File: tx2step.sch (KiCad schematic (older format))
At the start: 59 parts, among them CON1 BARREL_JACK, IC1 TPS2113A, IC3 MCP73831, IC4 TPS61202, IC5 DRV8834, IC6 DRV8834, J1 8P8C, J2 6P4C, J3 6P4C, J4 Debug, SW1 SW_DIP_x02, SW2 SW_DPDT_x2, SW3 SW_SPDT_MSM, U1 ATmega328P-MMH, Y1 16 MHz

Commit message: Use SPST for power switch
Add pullup resistor, unit is powered on when switch is open; off
when closed.
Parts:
- removed SW2: SW_DPDT_x2, symbol tx2step-rescue:SW_DPDT_x2
- added R4: 4.7KΩ, symbol Device:R_Small
- added SW2: SW_SPST, symbol Switch:SW_SPST
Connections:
- wire segments 287 -> 288
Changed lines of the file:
@@
-$EndComp
-$Comp
-L tx2step-rescue:SW_DPDT_x2 SW2
-U 1 1 58BE4643
-P 3700 6400
-F 0 "SW2" H 3700 6570 50  0000 C CNN
-F 1 "SW_DPDT_x2" H 3700 6200 50  0000 C CNN
-F 2 "" H 3700 6400 50  0001 C CNN
-F 3 "" H 3700 6400 50  0001 C CNN
-	1    3700 6400
-	-1   0    0    -1
 $EndComp
 $Comp
@@
 	3250 6550 3250 6500
 Wire Wire Line
-	3100 6800 3500 6800
-Wire Wire Line
 	3100 6550 3100 6800
 Connection ~ 4100 6800
@@
 Wire Wire Line
 	3900 6400 4300 6400
-Wire Wire Line
-	3500 6500 3500 6800
 Wire Wire Line
 	4700 5750 4200 5750
@@
 Connection ~ 6200 6300
 Wire Wire Line
-	3500 6800 4100 6800
-Connection ~ 3500 6800
-Wire Wire Line
-	3500 6300 3500 6200
-Connection ~ 3500 6200
-Wire Wire Line
 	2800 1800 2950 1800
 Wire Wire Line
@@
 	4200 6800 4300 6800
 Wire Wire Line
-	3250 6200 3500 6200
-Wire Wire Line
 	2950 6200 3250 6200
 Wire Wire Line
@@
 Wire Wire Line
 	6200 6300 6400 6300
-Wire Wire Line
-	3500 6200 4050 6200
 Wire Wire Line
 	2950 1800 3050 1800
@@
 Text Label 2700 4250 0    60   ~ 0
 DC_SENSE
+Wire Wire Line
+	3100 6800 3500 6800
+$Comp
+L Switch:SW_SPST SW2
+U 1 1 6347EBFA
+P 3700 6700
+F 0 "SW2" H 3700 6935 50  0000 C CNN
+F 1 "SW_SPST" H 3700 6844 50  0000 C CNN
+F 2 "" H 3700 6700 50  0001 C CNN
+F 3 "~" H 3700 6700 50  0001 C CNN
+	1    3700 6700
+	1    0    0    -1
+$EndComp
+Wire Wire Line
+	3900 6400 3900 6700
+Wire Wire Line
+	3500 6700 3500 6800
+Connection ~ 3500 6800
+Wire Wire Line
+	3500 6800 4100 6800
+Wire Wire Line
+	3250 6200 3500 6200
+$Comp
+L Device:R_Small R4
+U 1 1 635AA68E
+P 3500 6300
+F 0 "R4" H 3559 6346 50  0000 L CNN
+F 1 "4.7KΩ" H 3559 6255 50  0000 L CNN
+F 2 "" H 3500 6300 50  0001 C CNN
+F 3 "~" H 3500 6300 50  0001 C CNN
+	1    3500 6300
+	1    0    0    -1
+$EndComp
+Connection ~ 3500 6200
+Wire Wire Line
+	3500 6200 4050 6200
+Wire Wire Line
+	3500 6400 3900 6400
+Connection ~ 3900 6400
 $EndSCHEMATC

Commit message: Replace switches with pin header
This allows the switches to be mounted on the chassis, freeing up
space on the board and allowing for component flexibility.
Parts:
- removed RV1: POT, symbol tx2step-rescue:POT
- removed SW2: SW_SPST, symbol Switch:SW_SPST
- removed SW3: SW_SPDT_MSM, symbol tx2step-rescue:SW_SPDT_MSM
- added J5: CHASSIS_SWITCHES, symbol Connector_Generic:Conn_02x04_Odd_Even
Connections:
- net labels added: SW_POWER
- wire segments 288 -> 295
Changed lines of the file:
@@
-$EndComp
-$Comp
-L tx2step-rescue:SW_SPDT_MSM SW3
-U 1 1 58B86814
-P 5100 1000
-F 0 "SW3" H 5100 1200 50  0000 C CNN
-F 1 "SW_SPDT_MSM" H 5100 800 50  0000 C CNN
-F 2 "" H 5100 1000 50  0001 C CNN
-F 3 "" H 5100 1000 50  0001 C CNN
-	1    5100 1000
-	1    0    0    -1
-$EndComp
-$Comp
-L tx2step-rescue:POT RV1
-U 1 1 58B868AD
-P 5950 1000
-F 0 "RV1" V 5775 1000 50  0000 C CNN
-F 1 "POT" V 5850 1000 50  0000 C CNN
-F 2 "" H 5950 1000 50  0000 C CNN
-F 3 "" H 5950 1000 50  0000 C CNN
-	1    5950 1000
-	1    0    0    -1
-$EndComp
-$Comp
-L tx2step-rescue:GND #PWR025
-U 1 1 58B87520
-P 5950 1150
-F 0 "#PWR025" H 5950 900 50  0001 C CNN
-F 1 "GND" H 5950 1000 50  0000 C CNN
-F 2 "" H 5950 1150 50  0000 C CNN
-F 3 "" H 5950 1150 50  0000 C CNN
-	1    5950 1150
-	1    0    0    -1
 $EndComp
 $Comp
@@
 Connection ~ 2950 6200
 Wire Wire Line
-	3900 6400 4300 6400
-Wire Wire Line
 	4700 5750 4200 5750
 Wire Wire Line
@@
 Wire Wire Line
 	2000 850  2000 950
-$Comp
-L power:VCC #PWR024
-U 1 1 5FE50164
-P 5950 850
-F 0 "#PWR024" H 5950 700 50  0001 C CNN
-F 1 "VCC" H 5965 1023 50  0000 C CNN
-F 2 "" H 5950 850 50  0001 C CNN
-F 3 "" H 5950 850 50  0001 C CNN
-	1    5950 850
-	1    0    0    -1
-$EndComp
 $Comp
 L power:VCC #PWR032
@@
 	1    0    0    -1
 $EndComp
-Wire Wire Line
-	4700 1000 4900 1000
 Connection ~ 4700 1000
 $Comp
@@
 Wire Wire Line
 	4550 1000 4700 1000
-Wire Wire Line
-	6100 1000 6250 1000
-Text Label 6250 1000 0    60   ~ 0
-GUIDE_RATE
 Text Label 4550 1000 2    60   ~ 0
 TRACK_RATE
@@
 	1    0    0    -1
 $EndComp
-Wire Wire Line
-	5300 900  5400 900
-Wire Wire Line
-	5400 900  5400 850
-Wire Wire Line
-	5300 1100 5400 1100
-Wire Wire Line
-	5400 1100 5400 1250
-$Comp
-L power:GND #PWR031
-U 1 1 6325C28F
-P 5400 1250
-F 0 "#PWR031" H 5400 1000 50  0001 C CNN
-F 1 "GND" H 5405 1077 50  0000 C CNN
-F 2 "" H 5400 1250 50  0001 C CNN
-F 3 "" H 5400 1250 50  0001 C CNN
-	1    5400 1250
-	1    0    0    -1
-$EndComp
-$Comp
-L power:VCC #PWR022
-U 1 1 6325D155
-P 5400 850
-F 0 "#PWR022" H 5400 700 50  0001 C CNN
-F 1 "VCC" H 5415 1023 50  0000 C CNN
-F 2 "" H 5400 850 50  0001 C CNN
-F 3 "" H 5400 850 50  0001 C CNN
-	1    5400 850
-	1    0    0    -1
-$EndComp
 Connection ~ 2000 950
 Connection ~ 2000 1150
@@
 Text Label 2700 4250 0    60   ~ 0
 DC_SENSE
-Wire Wire Line
-	3100 6800 3500 6800
-$Comp
-L Switch:SW_SPST SW2
-U 1 1 6347EBFA
-P 3700 6700
-F 0 "SW2" H 3700 6935 50  0000 C CNN
-F 1 "SW_SPST" H 3700 6844 50  0000 C CNN
-F 2 "" H 3700 6700 50  0001 C CNN
-F 3 "~" H 3700 6700 50  0001 C CNN
-	1    3700 6700
-	1    0    0    -1
-$EndComp
-Wire Wire Line
-	3900 6400 3900 6700
-Wire Wire Line
-	3500 6700 3500 6800
-Connection ~ 3500 6800
-Wire Wire Line
-	3500 6800 4100 6800
 Wire Wire Line
 	3250 6200 3500 6200
@@
 Wire Wire Line
 	3500 6200 4050 6200
+$Comp
+L Connector_Generic:Conn_02x04_Odd_Even J5
+U 1 1 635FE306
+P 5950 1000
+F 0 "J5" H 6000 1317 50  0000 C CNN
+F 1 "CHASSIS_SWITCHES" H 6000 1226 50  0000 C CNN
+F 2 "" H 5950 1000 50  0001 C CNN
+F 3 "~" H 5950 1000 50  0001 C CNN
+	1    5950 1000
+	1    0    0    -1
+$EndComp
+Wire Wire Line
+	6250 1000 6350 1000
+Wire Wire Line
+	5750 1000 5650 1000
+Text Label 6350 1000 0    60   ~ 0
+GUIDE_RATE
+Text Label 5650 1000 2    60   ~ 0
+TRACK_RATE
+Text Label 6350 1200 0    60   ~ 0
+SW_POWER
+Wire Wire Line
+	6350 1200 6250 1200
+Wire Wire Line
+	5750 1200 5650 1200
+$Comp
+L power:GND #PWR025
+U 1 1 636F7BE1
+P 5650 1200
+F 0 "#PWR025" H 5650 950 50  0001 C CNN
+F 1 "GND" H 5655 1027 50  0000 C CNN
+F 2 "" H 5650 1200 50  0001 C CNN
+F 3 "" H 5650 1200 50  0001 C CNN
+	1    5650 1200
+	1    0    0    -1
+$EndComp
+Wire Wire Line
+	6250 900  6450 900
+Wire Wire Line
+	6450 900  6450 650
+Wire Wire Line
+	6450 650  6550 650
+Wire Wire Line
+	5750 900  5550 900
+Wire Wire Line
+	5550 900  5550 650
+Wire Wire Line
+	5550 650  5450 650
+$Comp
+L power:GND #PWR031
+U 1 1 63769B7F
+P 6550 650
+F 0 "#PWR031" H 6550 400 50  0001 C CNN
+F 1 "GND" H 6555 477 50  0000 C CNN
+F 2 "" H 6550 650 50  0001 C CNN
+F 3 "" H 6550 650 50  0001 C CNN
+	1    6550 650
+	1    0    0    -1
+$EndComp
+$Comp
+L power:GND #PWR024
+U 1 1 6376A908
+P 5450 650
+F 0 "#PWR024" H 5450 400 50  0001 C CNN
+F 1 "GND" H 5455 477 50  0000 C CNN
+F 2 "" H 5450 650 50  0001 C CNN
+F 3 "" H 5450 650 50  0001 C CNN
+	1    5450 650
+	1    0    0    -1
+$EndComp
+Wire Wire Line
+	5750 1100 5500 1100
+$Comp
+L power:VCC #PWR046
+U 1 1 637A432D
+P 7000 1100
+F 0 "#PWR046" H 7000 950 50  0001 C CNN
+F 1 "VCC" H 7015 1273 50  0000 C CNN
+F 2 "" H 7000 1100 50  0001 C CNN
+F 3 "" H 7000 1100 50  0001 C CNN
+	1    7000 1100
+	1    0    0    -1
+$EndComp
+$Comp
+L power:VCC #PWR022
+U 1 1 637A531E
+P 5300 1250
+F 0 "#PWR022" H 5300 1100 50  0001 C CNN
+F 1 "VCC" H 5315 1423 50  0000 C CNN
+F 2 "" H 5300 1250 50  0001 C CNN
+F 3 "" H 5300 1250 50  0001 C CNN
+	1    5300 1250
+	1    0    0    -1
+$EndComp
+Wire Wire Line
+	5300 1250 5500 1250
+Wire Wire Line
+	5500 1100 5500 1250
+Wire Wire Line
+	6250 1100 7000 1100
+Wire Wire Line
+	3100 6800 4100 6800
 Wire Wire Line
 	3500 6400 3900 6400
+Text Label 3850 6650 2    60   ~ 0
+SW_POWER
+Wire Wire Line
+	3850 6650 3900 6650
+Wire Wire Line
+	3900 6650 3900 6400
 Connection ~ 3900 6400
+Wire Wire Line
+	3900 6400 4300 6400
 $EndSCHEMATC

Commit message: Delete rescue lib
Remap all symbols to proper libraries
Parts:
- BT1: symbol tx2step-rescue:Battery_Cell -> Device:Battery_Cell
- C1, C10, C11, C12, C13, C14, C15, C16, C19, C20, C21, C22, C3, C4, C5, C6, C7, C8, C9: symbol tx2step-rescue:C_Small -> Device:C_Small
- C17, C18, C2: symbol tx2step-rescue:CP_Small -> Device:CP_Small
- D2: symbol tx2step-rescue:LED -> Device:LED
- D3, D4: symbol tx2step-rescue:LED_Small -> Device:LED_Small
- D5, D6, D7, D8: symbol tx2step-rescue:D_TVS -> Device:D_TVS
- IC1: symbol tx2step-rescue:TPS2113A -> tx2step:TPS2113A
- IC3: symbol tx2step-rescue:MCP73831 -> tx2step:MCP73831
- IC4: symbol tx2step-rescue:TPS61202 -> tx2step:TPS61202
- IC5, IC6: symbol tx2step-rescue:DRV8834 -> tx2step:DRV8834
- L1: symbol tx2step-rescue:L -> Device:L
- R1, R13, R14, R19, R20, R5, R6, R7, R8: symbol tx2step-rescue:R_Small -> Device:R_Small
- SW1: symbol tx2step-rescue:SW_DIP_x02 -> Switch:SW_DIP_x02
- Y1: symbol tx2step-rescue:Crystal -> Device:Crystal

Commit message: Assign initial footprints
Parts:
- BT1: footprint (none) -> Battery:Battery_Clip_21700
- C1, C10, C11, C12, C13, C14, C15, C16, C17, C18, C19, C2, C20, C21, C22, C3, C4, C5, C6, C7, C8, C9: footprint (none) -> Capacitor_SMD:C_0603_1608Metric
- CON1: footprint (none) -> Connector_BarrelJack:BarrelJack_Horizontal
- D2, D3, D4: footprint (none) -> LED_SMD:LED_0603_1608Metric
- D5, D6, D7, D8: footprint (none) -> Diode_SMD:D_0603_1608Metric
- IC1: footprint (none) -> Package_SON:Texas_S-PVSON-N8_ThermalVias
- IC3: footprint (none) -> Package_TO_SOT_SMD:SOT-23-5
- IC4: footprint (none) -> Package_SON:Texas_S-PVSON-N10_ThermalVias
- IC5, IC6: footprint (none) -> Package_DFN_QFN:QFN-24-1EP_4x4mm_P0.5mm_EP2.6x2.6mm_ThermalVias
- J1: footprint (none) -> Connector_RJ:RJ45_Amphenol_54602-x08_Horizontal
- J2, J3: footprint (none) -> Connector_RJ:RJ12_Amphenol_54601
- J4: footprint (none) -> Connector_PCBEdge:PCB_Edge_02x05
- J5: footprint (none) -> Connector_PinHeader_2.54mm:PinHeader_2x04_P2.54mm_Vertical
- L1: footprint (none) -> Inductor_SMD:L_1206_3216Metric
- R1, R13, R14, R19, R2, R20, R3, R4, R5, R6, R7, R8: footprint (none) -> Resistor_SMD:R_0805_2012Metric
- SW1: footprint (none) -> Package_DIP:DIP-4_W7.62mm
- Y1: footprint (none) -> Crystal:Crystal_SMD_2012-2Pin_2.0x1.2mm

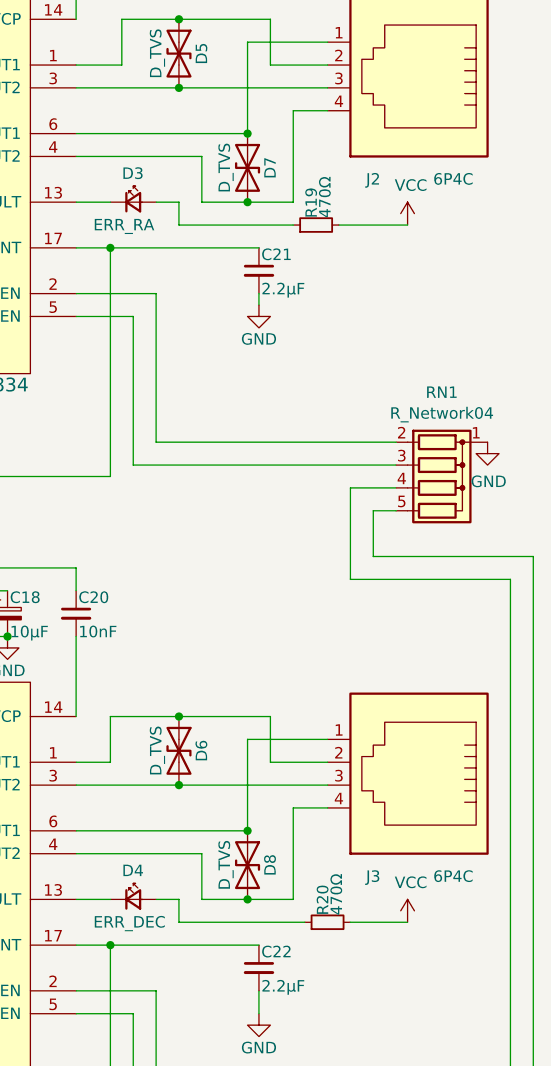
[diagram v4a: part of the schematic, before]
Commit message: Use multi-part component for combined 6P4C jack
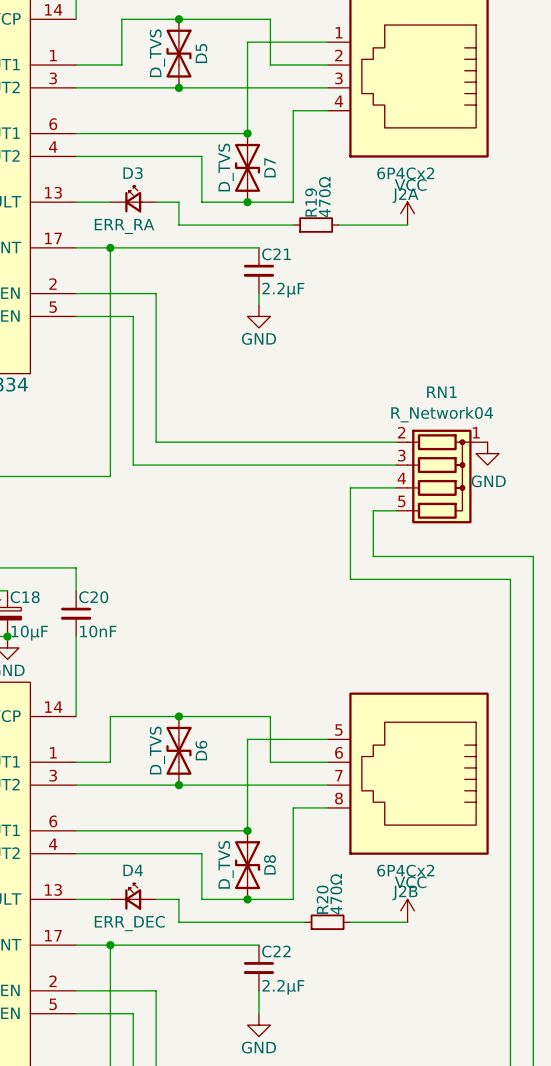
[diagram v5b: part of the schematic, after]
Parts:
- removed J2, J3: 6P4C, Connector_RJ:RJ12_Amphenol_54601, symbol Connector:6P4C
- added J2: 6P4Cx2, Connector_Multicomp:6P4Cx2, symbol tx2step:6P4Cx2
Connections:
- net at D7.1 (A1), IC5.6 (BOUT1): now also J2.1
- net at D5.1 (A1), IC5.1 (AOUT1): now also J2.2
- net at D5.2 (A2), IC5.3 (AOUT2): now also J2.3
- net at D7.2 (A2), IC5.4 (BOUT2): now also J2.4
- net at D8.1 (A1), IC6.6 (BOUT1): now also J2.5
- net at D6.1 (A1), IC6.1 (AOUT1): now also J2.6
- net at D6.2 (A2), IC6.3 (AOUT2): now also J2.7
- net at D8.2 (A2), IC6.4 (BOUT2): now also J2.8
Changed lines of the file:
@@
 $EndDescr
-$Comp
-L Connector:6P4C J2
-U 1 1 58B5172F
-P 9950 1600
-F 0 "J2" H 10150 2100 50  0000 C CNN
-F 1 "6P4C" H 9800 2100 50  0000 C CNN
-F 2 "Connector_RJ:RJ12_Amphenol_54601" H 9950 1600 50  0001 C CNN
-F 3 "" H 9950 1600 50  0000 C CNN
-	1    9950 1600
-	-1   0    0    1
-$EndComp
 $Comp
 L Device:D_TVS D5
@@
 	1    9200 2050
 	0    1    1    0
-$EndComp
-$Comp
-L Connector:6P4C J3
-U 1 1 58B53180
-P 9950 4650
-F 0 "J3" H 10150 5150 50  0000 C CNN
-F 1 "6P4C" H 9800 5150 50  0000 C CNN
-F 2 "Connector_RJ:RJ12_Amphenol_54601" H 9950 4650 50  0001 C CNN
-F 3 "" H 9950 4650 50  0000 C CNN
-	1    9950 4650
-	-1   0    0    1
 $EndComp
 $Comp
@@
 Wire Wire Line
 	3900 6400 4300 6400
+$Comp
+L tx2step:6P4Cx2 J2
+U 1 1 5FB324B3
+P 9950 1600
+F 0 "J2" H 10007 2167 50  0000 C CNN
+F 1 "6P4Cx2" H 10007 2076 50  0000 C CNN
+F 2 "Connector_Multicomp:6P4Cx2" V 9950 1625 50  0001 C CNN
+F 3 "~" V 9950 1625 50  0001 C CNN
+	1    9950 1600
+	-1   0    0    1
+$EndComp
+$Comp
+L tx2step:6P4Cx2 J2
+U 2 1 5FB33FF1
+P 9950 4650
+F 0 "J2" H 10007 5217 50  0000 C CNN
+F 1 "6P4Cx2" H 10007 5126 50  0000 C CNN
+F 2 "Connector_Multicomp:6P4Cx2" V 9950 4675 50  0001 C CNN
+F 3 "~" V 9950 4675 50  0001 C CNN
+	2    9950 4650
+	-1   0    0    1
+$EndComp
 $EndSCHEMATC

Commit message: Update footprints from BOM
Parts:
- C2: footprint Capacitor_SMD:C_0603_1608Metric -> Capacitor_THT:CP_Radial_D6.3mm_P2.50mm
- D5, D6, D7, D8: footprint Diode_SMD:D_0603_1608Metric -> Diode_SMD:D_SOD-323
- L1: footprint Inductor_SMD:L_1206_3216Metric -> Inductor_SMD:L_1008_2520Metric
- Y1: footprint Crystal:Crystal_SMD_2012-2Pin_2.0x1.2mm -> Crystal:Crystal_SMD_3225-4Pin_3.2x2.5mm; symbol Device:Crystal -> Device:Crystal_GND24
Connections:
- net GND: now also Y1.2, Y1.4
- net XTAL2: now also Y1.3; no longer Y1.2
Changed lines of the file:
@@
 F 0 "D5" H 8900 1650 50  0000 C CNN
 F 1 "D_TVS" H 8900 1450 50  0000 C CNN
-F 2 "Diode_SMD:D_0603_1608Metric" H 8900 1550 50  0001 C CNN
+F 2 "Diode_SMD:D_SOD-323" H 8900 1550 50  0001 C CNN
 F 3 "" H 8900 1550 50  0000 C CNN
 	1    8900 1550
@@
 F 0 "D7" H 9200 2150 50  0000 C CNN
 F 1 "D_TVS" H 9200 1950 50  0000 C CNN
-F 2 "Diode_SMD:D_0603_1608Metric" H 9200 2050 50  0001 C CNN
+F 2 "Diode_SMD:D_SOD-323" H 9200 2050 50  0001 C CNN
 F 3 "" H 9200 2050 50  0000 C CNN
 	1    9200 2050
@@
 F 0 "D6" H 8900 4700 50  0000 C CNN
 F 1 "D_TVS" H 8900 4500 50  0000 C CNN
-F 2 "Diode_SMD:D_0603_1608Metric" H 8900 4600 50  0001 C CNN
+F 2 "Diode_SMD:D_SOD-323" H 8900 4600 50  0001 C CNN
 F 3 "" H 8900 4600 50  0000 C CNN
 	1    8900 4600
@@
 F 0 "D8" H 9200 5200 50  0000 C CNN
 F 1 "D_TVS" H 9200 5000 50  0000 C CNN
-F 2 "Diode_SMD:D_0603_1608Metric" H 9200 5100 50  0001 C CNN
+F 2 "Diode_SMD:D_SOD-323" H 9200 5100 50  0001 C CNN
 F 3 "" H 9200 5100 50  0000 C CNN
 	1    9200 5100
@@
 $EndComp
 $Comp
-L Device:Crystal Y1
+L Device:Crystal_GND24 Y1
 U 1 1 58B8A677
 P 4800 1950
 F 0 "Y1" H 4800 2100 50  0000 C CNN
 F 1 "16 MHz" H 4800 1800 50  0000 C CNN
-F 2 "Crystal:Crystal_SMD_2012-2Pin_2.0x1.2mm" H 4800 1950 50  0001 C CNN
+F 2 "Crystal:Crystal_SMD_3225-4Pin_3.2x2.5mm" H 4800 1950 50  0001 C CNN
 F 3 "" H 4800 1950 50  0000 C CNN
 	1    4800 1950
@@
 F 0 "C2" H 2010 1120 50  0000 L CNN
 F 1 "47µF" H 2010 970 50  0000 L CNN
-F 2 "Capacitor_SMD:C_0603_1608Metric" H 2000 1050 50  0001 C CNN
+F 2 "Capacitor_THT:CP_Radial_D6.3mm_P2.50mm" H 2000 1050 50  0001 C CNN
 F 3 "" H 2000 1050 50  0000 C CNN
 	1    2000 1050
@@
 F 0 "L1" V 4800 5750 50  0000 C CNN
 F 1 "2.2µH" V 4925 5750 50  0000 C CNN
-F 2 "Inductor_SMD:L_1206_3216Metric" H 4850 5750 50  0001 C CNN
+F 2 "Inductor_SMD:L_1008_2520Metric" H 4850 5750 50  0001 C CNN
 F 3 "" H 4850 5750 50  0000 C CNN
 	1    4850 5750
@@
 	-1   0    0    1
 $EndComp
+$Comp
+L power:GND #PWR?
+U 1 1 5FAF93CA
+P 4350 2200
+F 0 "#PWR?" H 4350 1950 50  0001 C CNN
+F 1 "GND" H 4355 2027 50  0000 C CNN
+F 2 "" H 4350 2200 50  0001 C CNN
+F 3 "" H 4350 2200 50  0001 C CNN
+	1    4350 2200
+	1    0    0    -1
+$EndComp
+Wire Wire Line
+	4800 2150 4350 2150
+Wire Wire Line
+	4350 2150 4350 2200
+Wire Wire Line
+	4350 2150 4250 2150
+Wire Wire Line
+	4250 2150 4250 1700
+Wire Wire Line
+	4250 1700 4800 1700
+Wire Wire Line
+	4800 1700 4800 1750
+Connection ~ 4350 2150
 $EndSCHEMATC

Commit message: Use regular 6-pin ISP for reprogramming
Eliminate special edge connector that also exposes ST-4.
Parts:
- J4: value Debug -> Prog; footprint Connector_PCBEdge:PCB_Edge_02x05 -> Connector_PinHeader_2.54mm:PinHeader_2x03_P2.54mm_Vertical; symbol Connector_Generic:Conn_02x05_Odd_Even -> Connector_Generic:Conn_02x03_Odd_Even
- R1, R13, R14, R19, R2, R20, R3, R4, R5, R6, R7, R8: footprint Resistor_SMD:R_0805_2012Metric -> Resistor_SMD:R_0603_1608Metric
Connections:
- net JS_DEC: no longer J4.10 (Pin_10)
- net JS_RA: no longer J4.8 (Pin_8)
- net ST4_RA+: no longer J4.7 (Pin_7)
- no-connect marks 5 -> 4
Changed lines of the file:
@@
 F 0 "R13" H 6630 2720 50  0000 L CNN
 F 1 "47KΩ" H 6630 2660 50  0000 L CNN
-F 2 "Resistor_SMD:R_0805_2012Metric" H 6600 2700 50  0001 C CNN
+F 2 "Resistor_SMD:R_0603_1608Metric" H 6600 2700 50  0001 C CNN
 F 3 "" H 6600 2700 50  0000 C CNN
 	1    6600 2700
@@
 F 0 "R14" H 6630 5770 50  0000 L CNN
 F 1 "47KΩ" H 6630 5710 50  0000 L CNN
-F 2 "Resistor_SMD:R_0805_2012Metric" H 6600 5750 50  0001 C CNN
+F 2 "Resistor_SMD:R_0603_1608Metric" H 6600 5750 50  0001 C CNN
 F 3 "" H 6600 5750 50  0000 C CNN
 	1    6600 5750
@@
 F 0 "R6" H 3530 7420 50  0000 L CNN
 F 1 "2Ω" H 3530 7360 50  0000 L CNN
-F 2 "Resistor_SMD:R_0805_2012Metric" H 3500 7400 50  0001 C CNN
+F 2 "Resistor_SMD:R_0603_1608Metric" H 3500 7400 50  0001 C CNN
 F 3 "" H 3500 7400 50  0000 C CNN
 	1    3500 7400
@@
 F 0 "R1" H 930 6520 50  0000 L CNN
 F 1 "470Ω" H 930 6460 50  0000 L CNN
-F 2 "Resistor_SMD:R_0805_2012Metric" H 900 6500 50  0001 C CNN
+F 2 "Resistor_SMD:R_0603_1608Metric" H 900 6500 50  0001 C CNN
 F 3 "" H 900 6500 50  0000 C CNN
 	1    900  6500
@@
 F 0 "R5" H 2730 1020 50  0000 L CNN
 F 1 "1KΩ" H 2730 960 50  0000 L CNN
-F 2 "Resistor_SMD:R_0805_2012Metric" H 2700 1000 50  0001 C CNN
+F 2 "Resistor_SMD:R_0603_1608Metric" H 2700 1000 50  0001 C CNN
 F 3 "" H 2700 1000 50  0000 C CNN
 	1    2700 1000
@@
 F 0 "R19" H 9530 2320 50  0000 L CNN
 F 1 "470Ω" H 9530 2260 50  0000 L CNN
-F 2 "Resistor_SMD:R_0805_2012Metric" H 9500 2300 50  0001 C CNN
+F 2 "Resistor_SMD:R_0603_1608Metric" H 9500 2300 50  0001 C CNN
 F 3 "" H 9500 2300 50  0000 C CNN
 	1    9500 2300
@@
 F 0 "R20" H 9580 5370 50  0000 L CNN
 F 1 "470Ω" H 9580 5310 50  0000 L CNN
-F 2 "Resistor_SMD:R_0805_2012Metric" H 9550 5350 50  0001 C CNN
+F 2 "Resistor_SMD:R_0603_1608Metric" H 9550 5350 50  0001 C CNN
 F 3 "" H 9550 5350 50  0000 C CNN
 	1    9550 5350
@@
 F 0 "R8" H 4730 1120 50  0000 L CNN
 F 1 "4.7KΩ" H 4730 1060 50  0000 L CNN
-F 2 "Resistor_SMD:R_0805_2012Metric" H 4700 1100 50  0001 C CNN
+F 2 "Resistor_SMD:R_0603_1608Metric" H 4700 1100 50  0001 C CNN
 F 3 "" H 4700 1100 50  0000 C CNN
 	1    4700 1100
@@
 F 0 "R7" H 4730 920 50  0000 L CNN
 F 1 "4.7KΩ" H 4730 860 50  0000 L CNN
-F 2 "Resistor_SMD:R_0805_2012Metric" H 4700 900 50  0001 C CNN
+F 2 "Resistor_SMD:R_0603_1608Metric" H 4700 900 50  0001 C CNN
 F 3 "" H 4700 900 50  0000 C CNN
 	1    4700 900
@@
 F 0 "R2" H 1270 7296 50  0000 L CNN
 F 1 "4.7KΩ" H 1270 7205 50  0000 L CNN
-F 2 "Resistor_SMD:R_0805_2012Metric" V 1130 7250 50  0001 C CNN
+F 2 "Resistor_SMD:R_0603_1608Metric" V 1130 7250 50  0001 C CNN
 F 3 "~" H 1200 7250 50  0001 C CNN
 	1    1200 7250
@@
 F 0 "R3" H 1270 7596 50  0000 L CNN
 F 1 "4.7KΩ" H 1270 7505 50  0000 L CNN
-F 2 "Resistor_SMD:R_0805_2012Metric" V 1130 7550 50  0001 C CNN
+F 2 "Resistor_SMD:R_0603_1608Metric" V 1130 7550 50  0001 C CNN
 F 3 "~" H 1200 7550 50  0001 C CNN
 	1    1200 7550
@@
 Text Label 5150 4700 0    60   ~ 0
 ST4_DEC+
-Text Label 4450 4900 2    60   ~ 0
-ST4_RA+
-Wire Wire Line
-	4550 4900 4450 4900
-NoConn ~ 4550 5000
 $Comp
 L power:GND #PWR043
@@
 Wire Wire Line
 	3850 3400 4550 3400
-Text Label 5150 4900 0    60   ~ 0
-JS_RA
-Text Label 5150 5000 0    60   ~ 0
-JS_DEC
-Wire Wire Line
-	5050 5000 5150 5000
-Wire Wire Line
-	5050 4900 5150 4900
 Wire Wire Line
 	5050 4700 5150 4700
@@
 $EndComp
 $Comp
-L Connector_Generic:Conn_02x05_Odd_Even J4
+L Connector_Generic:Conn_02x03_Odd_Even J4
 U 1 1 5F99676C
-P 4750 4800
-F 0 "J4" H 4800 5217 50  0000 C CNN
-F 1 "Debug" H 4800 5126 50  0000 C CNN
-F 2 "Connector_PCBEdge:PCB_Edge_02x05" H 4750 4800 50  0001 C CNN
-F 3 "~" H 4750 4800 50  0001 C CNN
-	1    4750 4800
+P 4750 4700
+F 0 "J4" H 4800 5117 50  0000 C CNN
+F 1 "Prog" H 4800 5026 50  0000 C CNN
+F 2 "Connector_PinHeader_2.54mm:PinHeader_2x03_P2.54mm_Vertical" H 4750 4700 50  0001 C CNN
+F 3 "~" H 4750 4700 50  0001 C CNN
+	1    4750 4700
 	1    0    0    -1
 $EndComp
@@
 F 0 "R4" H 3559 6346 50  0000 L CNN
 F 1 "4.7KΩ" H 3559 6255 50  0000 L CNN
-F 2 "Resistor_SMD:R_0805_2012Metric" H 3500 6300 50  0001 C CNN
+F 2 "Resistor_SMD:R_0603_1608Metric" H 3500 6300 50  0001 C CNN
 F 3 "~" H 3500 6300 50  0001 C CNN
 	1    3500 6300
@@
 $EndComp
 $Comp
-L power:GND #PWR?
+L power:GND #PWR0101
 U 1 1 5FAF93CA
 P 4350 2200
-F 0 "#PWR?" H 4350 1950 50  0001 C CNN
+F 0 "#PWR0101" H 4350 1950 50  0001 C CNN
 F 1 "GND" H 4355 2027 50  0000 C CNN
 F 2 "" H 4350 2200 50  0001 C CNN
